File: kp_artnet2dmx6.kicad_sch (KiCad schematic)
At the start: 53 parts, among them IC1 KSZ8081MNXIA-TR, IC2 M95640-RMN6P, J1 RJ45_Amphenol_RJMG1BD3B8K1ANR, SW1 SW_SPDT, U1 STM32F407VETx, Y1 ASDDV-25.000MHZ-LC-T

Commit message: add mcp
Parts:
- added C22, C23, C24: 100n, symbol Device:C_Small
- added J2: SCREEN, Connector_JST:JST_XH_B4B-XH-A_1x04_P2.50mm_Vertical, symbol Connector_Generic:Conn_01x04
- added J3, J4, J5, J6: Conn_01x06, symbol Connector_Generic:Conn_01x06
- added U2: MCP23S17_SP, Package_DIP:DIP-28_W7.62mm, symbol Interface_Expansion:MCP23S17_SP
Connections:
- net +3.3V: now also C23.1, J3.2 (Pin_2), J4.2 (Pin_2), J5.2 (Pin_2), J6.2 (Pin_2), U2.9 (VDD)
- net GND: now also C22.2, C23.2, C24.2, J2.1 (Pin_1), J3.1 (Pin_1), J4.1 (Pin_1), J5.1 (Pin_1), J6.1 (Pin_1), U2.10 (VSS), U2.15 (A0), U2.16 (A1), U2.17 (A2)
- net STM_EEPROM_WRITE_GPIO: now also U1.58 (PD11); no longer U1.60 (PD13)
- net STM_NRST: now also C24.1
- net STM_SPI2_MISO: now also U2.14 (SO)
- net STM_SPI2_MOSI: now also U2.13 (SI)
- net STM_SPI2_NSS2_GPIO: now also U2.11 (~{CS})
- net STM_SPI2_SCK: now also U2.12 (SCK)
- net STM_MCP_INTA_GPIO: now reaches U1.61 (PD14)
- net STM_MCP_INTA_GPIO: now also U2.20 (INTA)
- net STM_MCP_INTB_GPIO: now reaches U1.62 (PD15)
- net STM_MCP_INTB_GPIO: now also U2.19 (INTB)
- net STM_I2C1_SCL: now reaches U1.92 (PB6)
- net STM_I2C1_SCL: now also J2.4 (Pin_4)
- net STM_I2C1_SDA: now reaches U1.93 (PB7)
- net STM_I2C1_SDA: now also J2.3 (Pin_3)
- new net +5V: C22.1, J2.2 (Pin_2)
- new net MCP_A0: J5.3 (Pin_3), U2.21 (GPA0)
- new net MCP_A1: J5.4 (Pin_4), U2.22 (GPA1)
- new net MCP_A2: J5.5 (Pin_5), U2.23 (GPA2)
- new net MCP_A3: J5.6 (Pin_6), U2.24 (GPA3)
- new net MCP_A4: J6.3 (Pin_3), U2.25 (GPA4)
- new net MCP_A5: J6.4 (Pin_4), U2.26 (GPA5)
- new net MCP_A6: J6.5 (Pin_5), U2.27 (GPA6)
- new net MCP_A7: J6.6 (Pin_6), U2.28 (GPA7)
- new net MCP_B0: J3.3 (Pin_3), U2.1 (GPB0)
- new net MCP_B1: J3.4 (Pin_4), U2.2 (GPB1)
- new net MCP_B2: J3.5 (Pin_5), U2.3 (GPB2)
- new net MCP_B3: J3.6 (Pin_6), U2.4 (GPB3)
- new net MCP_B4: J4.3 (Pin_3), U2.5 (GPB4)
- new net MCP_B5: J4.4 (Pin_4), U2.6 (GPB5)
- new net MCP_B6: J4.5 (Pin_5), U2.7 (GPB6)
- new net MCP_B7: J4.6 (Pin_6), U2.8 (GPB7)
- new net STM_MCP_RESET_GPIO: U1.60 (PD13), U2.18 (~{RESET})
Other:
- note added: "BTNS & LEDS"
- note added: "EEPROM"
- note added: "ETHERNET"
- note added: "NRST pin protection"
- note added: "SCREEN"
- note added: "STM"
- note added: "connectors farnell links : (maybe) on-wire connector https://fr.farnell.com/jst-japan-solderless-terminals/xhp-4/connecteur-male-4-voies/dp/1516266 straight on-board connector https://fr.farnell.com/jst-japan-solderless-terminals/b4b-xh-a-lf-sn/embase-male-vertical-4-voies/dp/1516278?MER=sy-me-pd-mi-acce 90deg on-board connector https://fr.farnell.com/jst-japan-solderless-terminals/s4b-xh-a-lf-sn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"
- moved on the sheet: C21, IC2, R19, R20

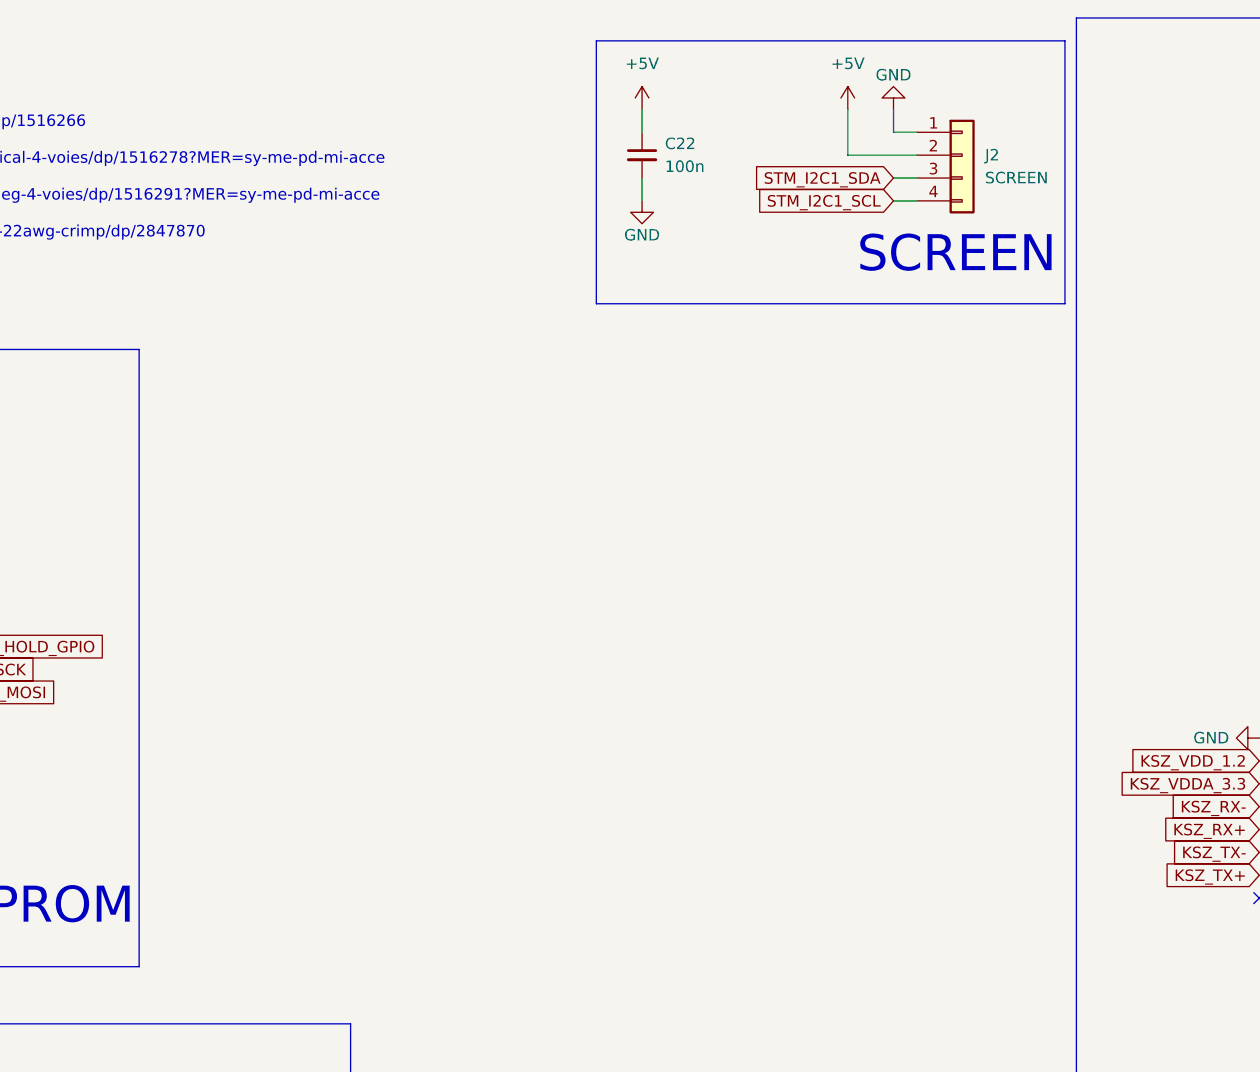
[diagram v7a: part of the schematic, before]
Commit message: add level shifter for i2c screen
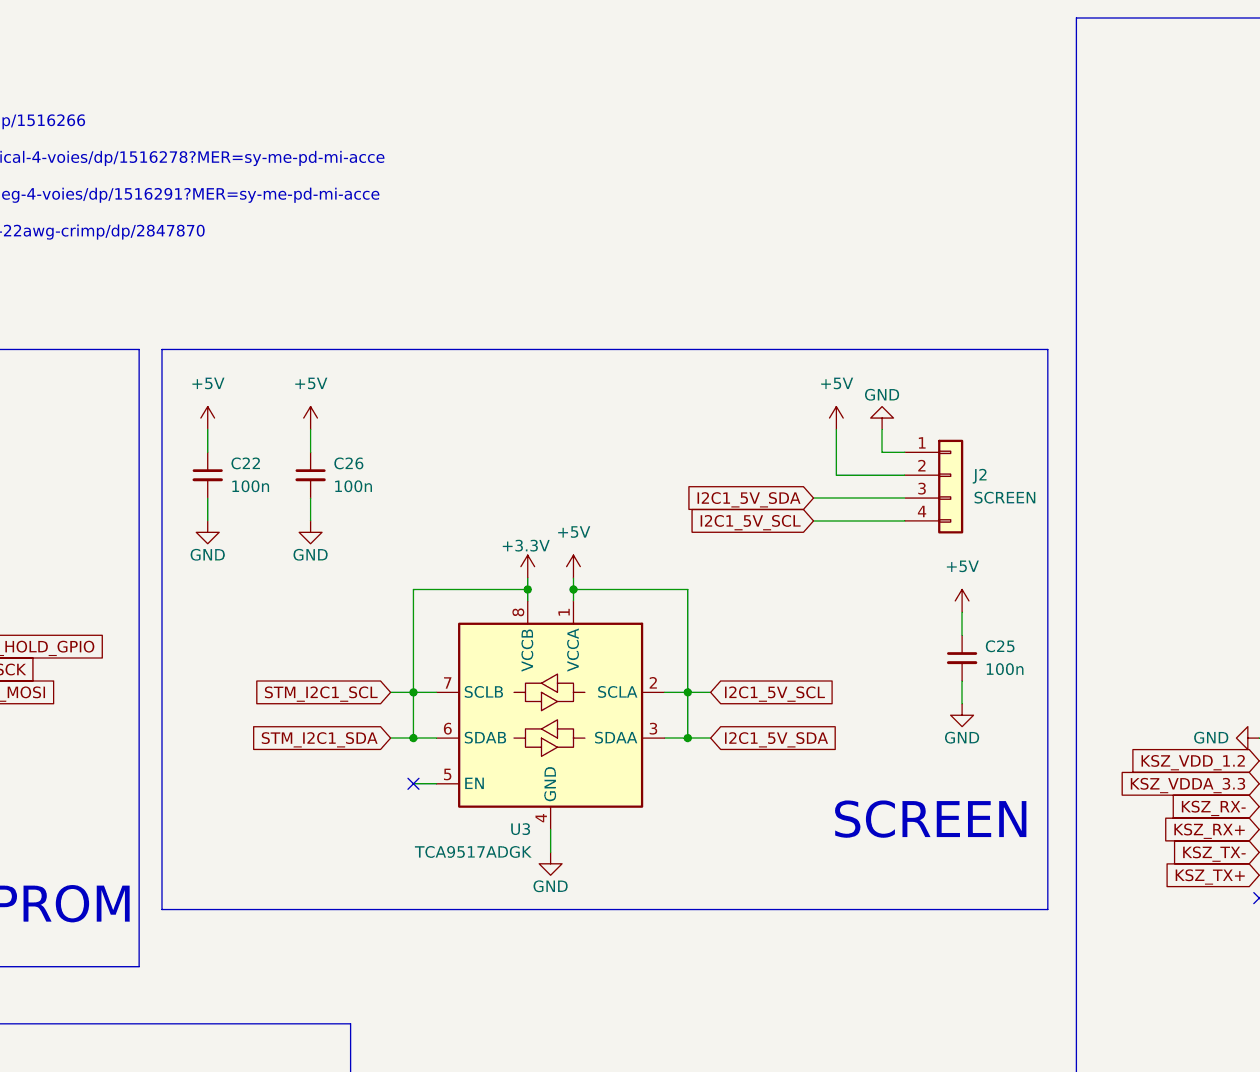
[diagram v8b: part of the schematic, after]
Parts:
- added C25, C26: 100n, symbol Device:C_Small
- added U3: TCA9517ADGK, Package_SO:VSSOP-8_3x3mm_P0.65mm, symbol Logic_LevelTranslator:TCA9517ADGK
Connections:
- net +3.3V: now also U1.92 (PB6), U1.93 (PB7), U3.6 (SDAB), U3.7 (SCLB), U3.8 (VCCB)
- net +5V: now also J2.3 (Pin_3), J2.4 (Pin_4), C25.1, C26.1, U3.1 (VCCA), U3.2 (SCLA), U3.3 (SDAA)
- net GND: now also C25.2, C26.2, U3.4 (GND)
- removed net STM_I2C1_SCL: J2.4 (Pin_4), U1.92 (PB6)
- removed net STM_I2C1_SDA: J2.3 (Pin_3), U1.93 (PB7)
- no-connect marks 3 -> 4
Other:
- moved on the sheet: C22, J2
